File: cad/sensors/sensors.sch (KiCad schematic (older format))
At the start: 65 parts

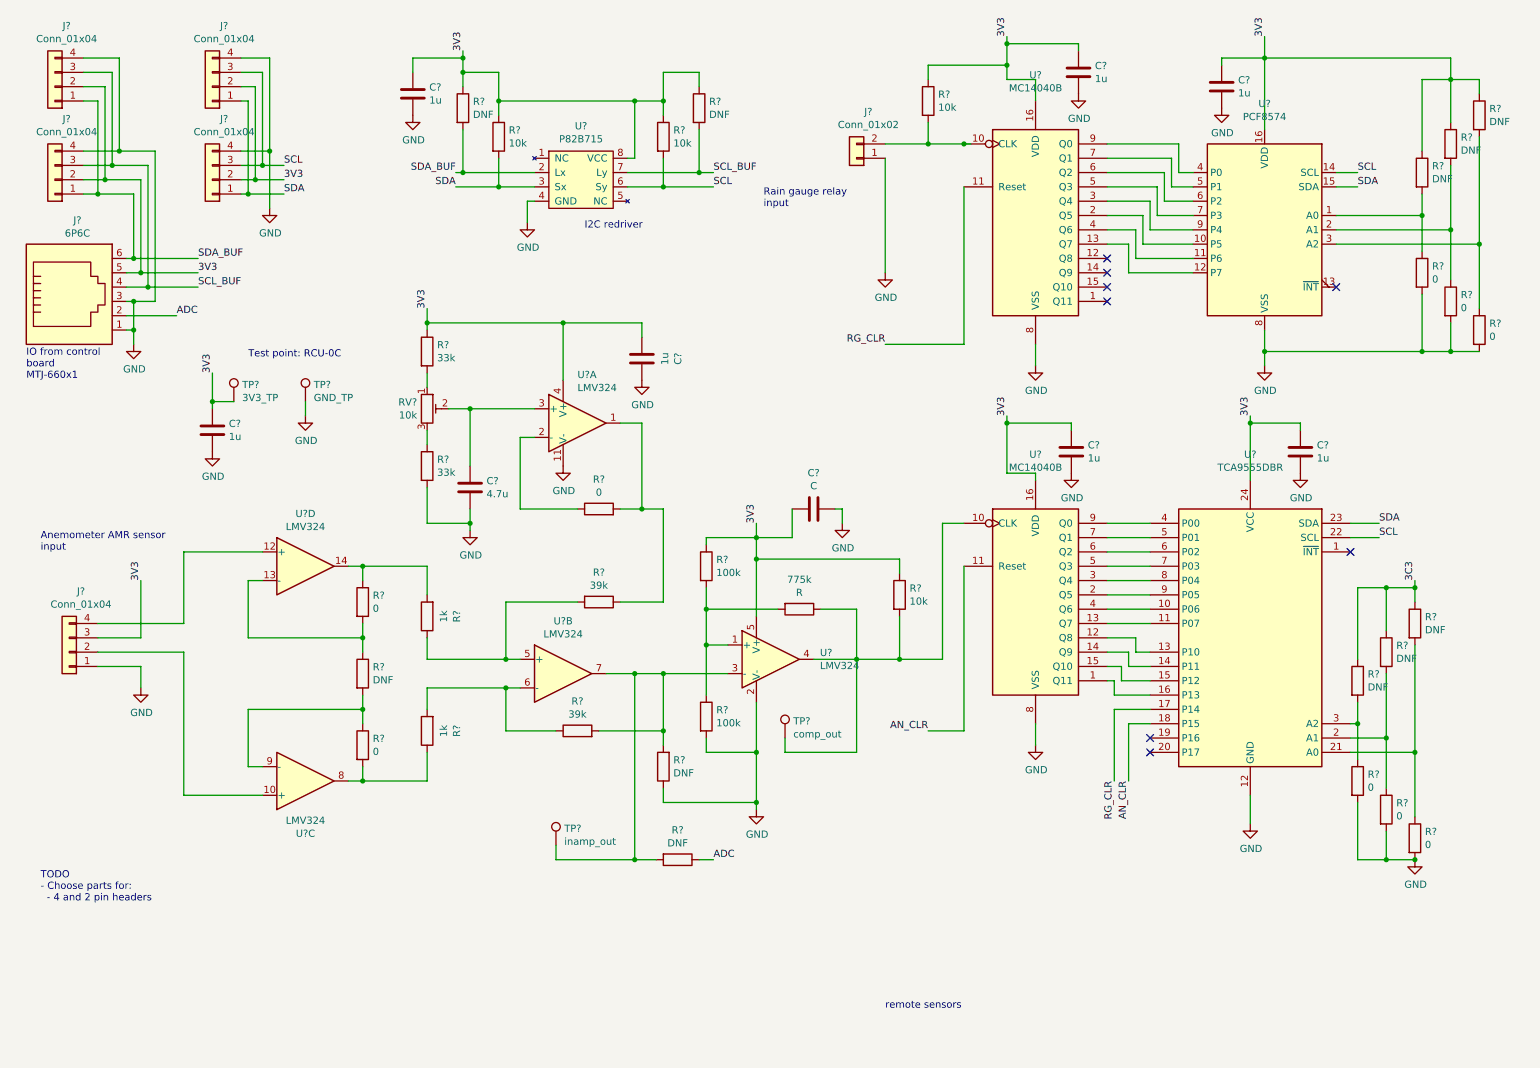
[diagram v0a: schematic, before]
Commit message: Added decoupling inductors and capacitors
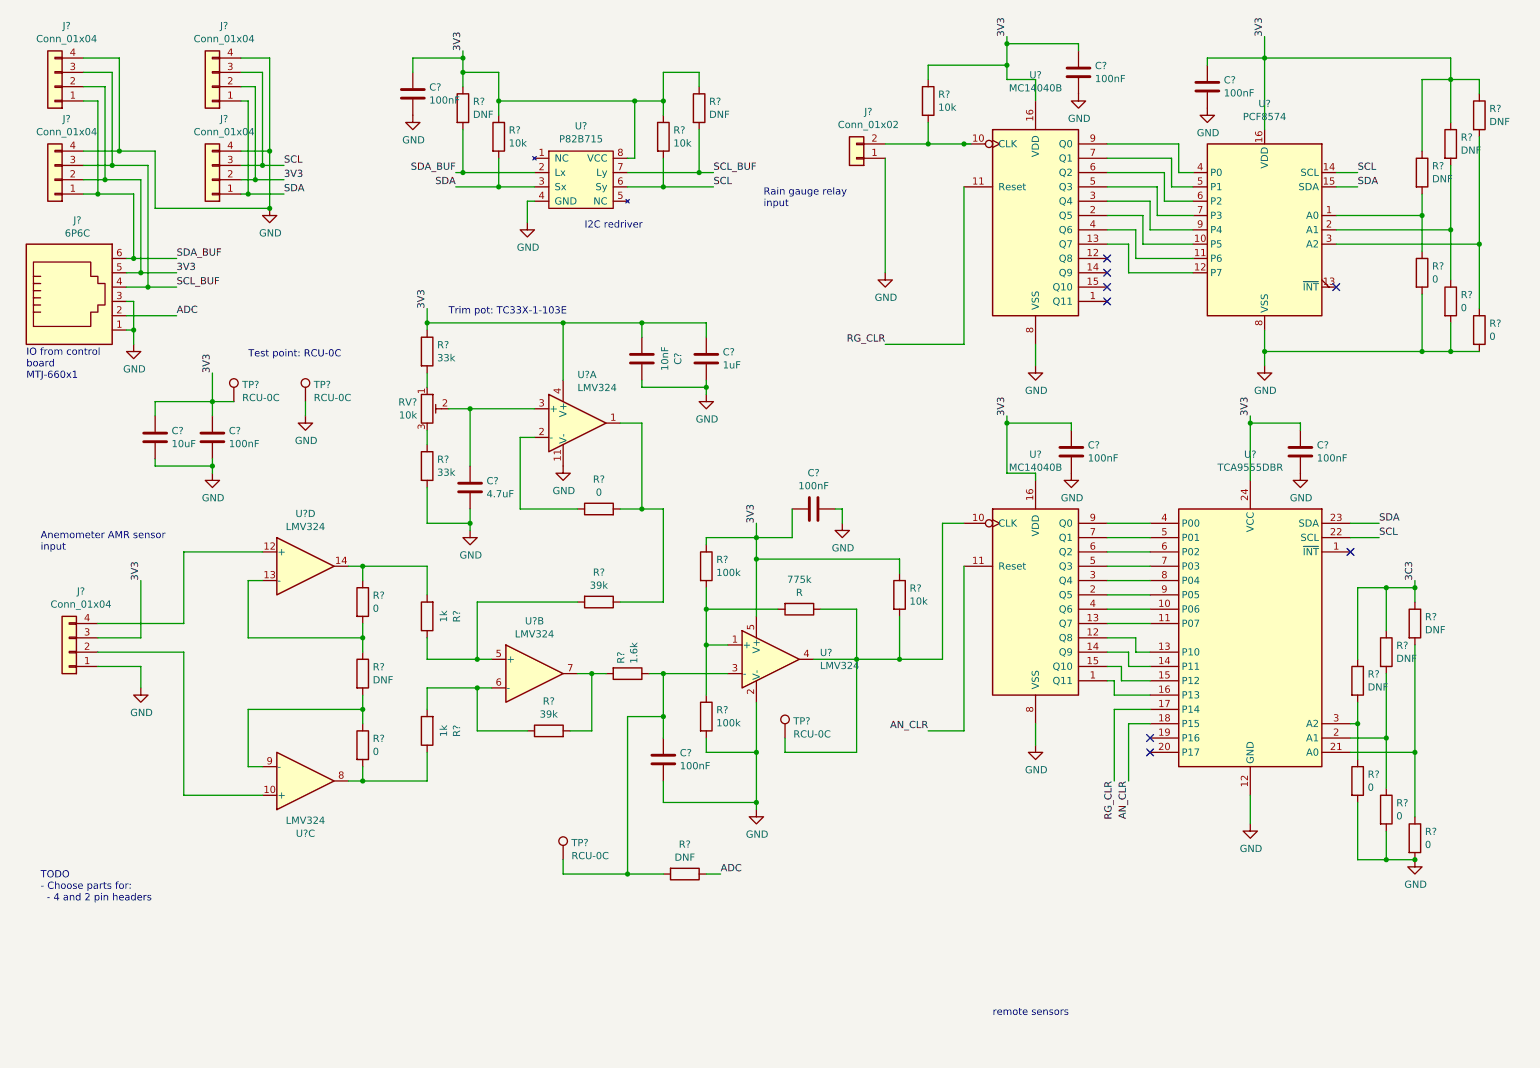
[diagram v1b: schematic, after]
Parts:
- removed R?: DNF, symbol Device:R
- added C?: 10uF, Capacitor_SMD:C_0603_1608Metric, symbol Device:C
- added C? (x2): 100nF, Capacitor_SMD:C_0603_1608Metric, symbol Device:C
- added R?: 1.6k, Resistor_SMD:R_0603_1608Metric, symbol Device:R
- 775k, R? (x31): footprint (none) -> Resistor_SMD:R_0603_1608Metric
- C?: value 1u -> 10nF; footprint (none) -> Capacitor_SMD:C_0603_1608Metric
- C?: value 4.7u -> 4.7uF; footprint (none) -> Capacitor_SMD:C_0603_1608Metric
- C?: value C -> 100nF; footprint (none) -> Capacitor_SMD:C_0603_1608Metric
- C? (x5): value 1u -> 100nF; footprint (none) -> Capacitor_SMD:C_0603_1608Metric
- C?: value 1u -> 1uF; footprint (none) -> Capacitor_SMD:C_0603_1608Metric
- TP?: value inamp_out -> RCU-0C
- TP?: value comp_out -> RCU-0C
- TP?: value 3V3_TP -> RCU-0C
- TP?: value GND_TP -> RCU-0C
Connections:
- net 3V3: now also C?.1, C?.1
- net GND: now also C?.1, C?.2, C?.2
- net at R?.2, TP?.1, U?.3 (-): now also C?.2, R?.1; no longer R?.2, U?.7
- new net: R?.2, R?.2, U?.7
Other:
- note added: "Trim pot: TC33X-1-103E"
- moved on the sheet: C?, R?, TP?, U?B

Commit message: Ordered components
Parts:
- R19: renamed from 775k; value R -> 775k
- U3: renamed from U?; value LMV324 -> LMV331
- gave numbers to parts that had none: 62

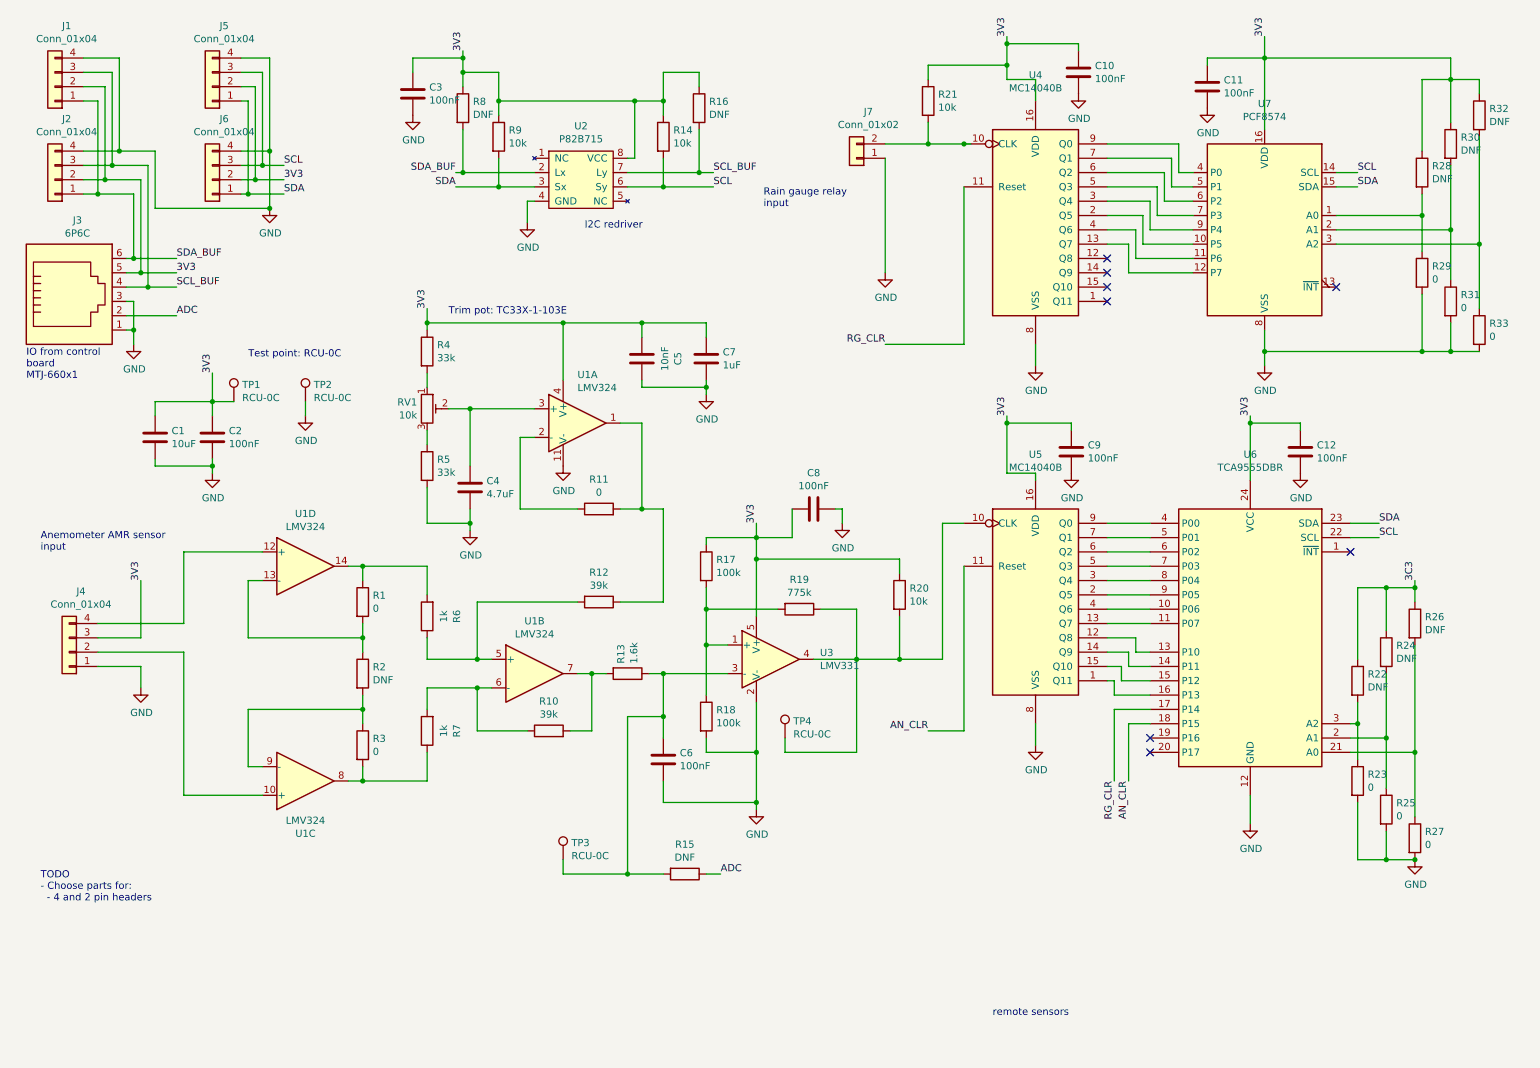
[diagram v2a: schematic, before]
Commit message: Changed I2C buffer to PCA1517, added termination network on RJ11 I2C lines
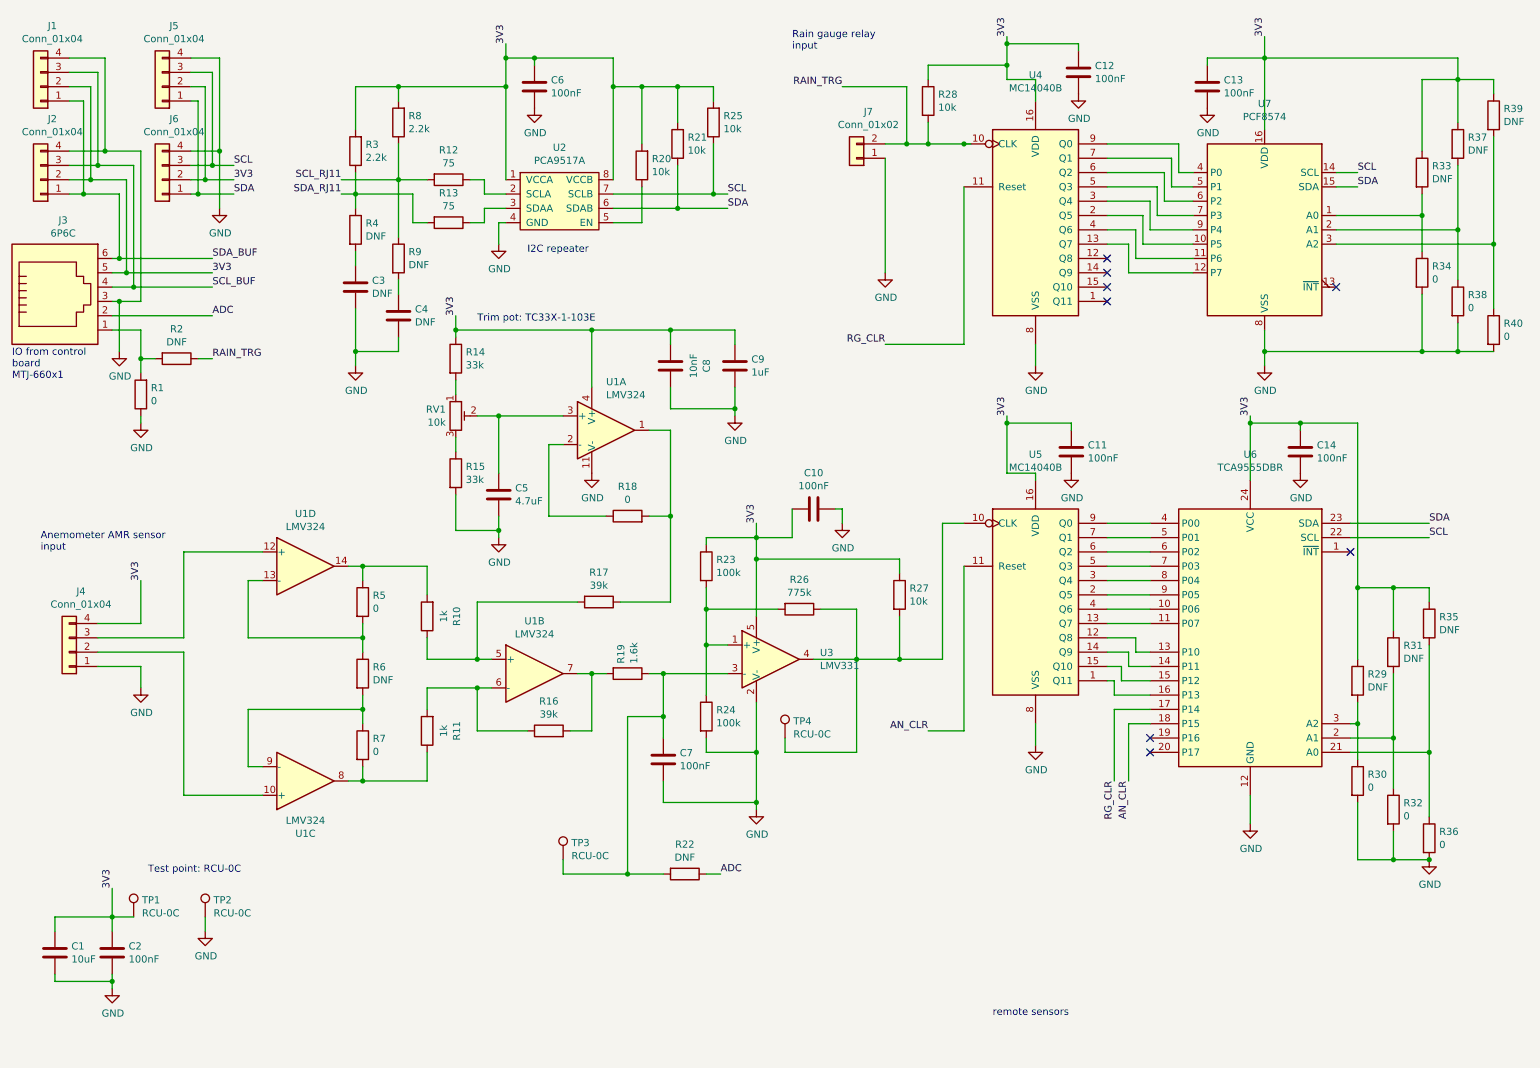
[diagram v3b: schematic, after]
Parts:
- removed R14: 10k, Resistor_SMD:R_0603_1608Metric, symbol Device:R
- removed R16: DNF, Resistor_SMD:R_0603_1608Metric, symbol Device:R
- removed U2: P82B715, symbol custom:P82B715
- added C4: DNF, Capacitor_SMD:C_0603_1608Metric, symbol Device:C
- added C6: 100nF, Capacitor_SMD:C_0603_1608Metric, symbol Device:C
- added R1: 0, Resistor_SMD:R_0603_1608Metric, symbol Device:R
- added R12, R13: 75, Resistor_SMD:R_0603_1608Metric, symbol Device:R
- added R2, R4: DNF, Resistor_SMD:R_0603_1608Metric, symbol Device:R
- added R20, R21, R25: 10k, Resistor_SMD:R_0603_1608Metric, symbol Device:R
- added R3: 2.2k, Resistor_SMD:R_0603_1608Metric, symbol Device:R
- added U2: PCA9517A, symbol custom:PCA9517A
- C3: value 100nF -> DNF
- R8: value DNF -> 2.2k
- R9: value 10k -> DNF
- renumbered C8 to C10, C9 to C11, C10 to C12, C11 to C13, C12 to C14, C4 to C5, C6 to C7, C5 to C8, C7 to C9, R6 to R10, R7 to R11, R4 to R14, R5 to R15, R10 to R16, R12 to R17, R11 to R18, R13 to R19, R15 to R22, R17 to R23, R18 to R24, R19 to R26, R20 to R27, R21 to R28, R22 to R29, R23 to R30, R24 to R31, R25 to R32, R28 to R33, R29 to R34, R26 to R35, R27 to R36, R30 to R37, R31 to R38, R32 to R39, R33 to R40, R1 to R5, R2 to R6, R3 to R7
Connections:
- net 3C3 is gone; now on net 3V3: R29.1, R31.1, R35.1
- net 3V3: now also J4.4 (Pin_4), R8.2, C6.1, R20.2, R21.2, R25.2, R3.2, U2.1 (VCCA), U2.8 (VCCB); no longer C3.2, J4.3 (Pin_3), R8.1, R9.1
- net GND: now also C3.2, C4.2, C6.2, R1.1, U2.4 (GND); no longer C3.1, J3.1
- net SCL: now also R25.1, U2.7 (SCLB)
- net SDA: now also R21.1, U2.6 (SDAB); no longer R9.2
- net SDA_BUF: no longer R8.2
- net RAIN_TRG: now reaches J7.2 (Pin_2), R28.2, U4.10 (CLK)
- net RAIN_TRG: now also R2.1
- net at U1.12 (+): now also J4.3 (Pin_3); no longer J4.4 (Pin_4)
- new net: J3.1, R1.2, R2.2
- new net: C4.1, R9.2
- new net: C3.1, R4.2
- new net: R12.1, U2.2 (SCLA)
- new net: R13.1, U2.3 (SDAA)
- new net: R20.1, U2.5 (EN)
- new net SCL_RJ11: R12.2, R8.1, R9.1
- new net SDA_RJ11: R13.2, R3.1, R4.1
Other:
- note added: "I2C repeater\n\n"
- note removed: "I2C redriver\n"
- note removed: "TODO\n- Choose parts for:\n - 4 and 2 pin headers"
- moved on the sheet: C1, C2, C5, C8, C9, J1, J2, J3, J5, J6, R14, R15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

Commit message: Final commit before moving to project repo
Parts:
- added C?: 100nF, Capacitor_SMD:C_0603_1608Metric, symbol Device:C
- added R?: 100k, Resistor_SMD:R_0603_1608Metric, symbol Device:R
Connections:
- net GND: now also C?.1
- net RAIN_TRG: now also C?.2, R?.1; no longer J7.2 (Pin_2), R28.2
- new net: J7.2 (Pin_2), R28.2, R?.2
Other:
- moved on the sheet: J7, R28
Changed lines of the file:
@@
 Wire Wire Line
 	7700 5450 7700 5600
-Wire Wire Line
-	7200 4350 7200 5500
 Text Label 7500 3300 1    50   ~ 0
 3V3
@@
 L Connector_Generic:Conn_01x02 J7
 U 1 1 6232698D
-P 6450 1500
-F 0 "J7" H 6368 1175 50  0000 C CNN
-F 1 "Conn_01x02" H 6368 1266 50  0000 C CNN
-F 2 "" H 6450 1500 50  0001 C CNN
-F 3 "~" H 6450 1500 50  0001 C CNN
-	1    6450 1500
+P 6000 1500
+F 0 "J7" H 5918 1175 50  0000 C CNN
+F 1 "Conn_01x02" H 5918 1266 50  0000 C CNN
+F 2 "" H 6000 1500 50  0001 C CNN
+F 3 "~" H 6000 1500 50  0001 C CNN
+	1    6000 1500
 	-1   0    0    1
 $EndComp
@@
 L power:GND #PWR015
 U 1 1 62326995
-P 6650 2300
-F 0 "#PWR015" H 6650 2050 50  0001 C CNN
-F 1 "GND" H 6655 2127 50  0000 C CNN
-F 2 "" H 6650 2300 50  0001 C CNN
-F 3 "" H 6650 2300 50  0001 C CNN
-	1    6650 2300
+P 6200 2300
+F 0 "#PWR015" H 6200 2050 50  0001 C CNN
+F 1 "GND" H 6205 2127 50  0000 C CNN
+F 2 "" H 6200 2300 50  0001 C CNN
+F 3 "" H 6200 2300 50  0001 C CNN
+	1    6200 2300
 	1    0    0    -1
 $EndComp
@@
 L Device:R R28
 U 1 1 6232699B
-P 6950 1100
-F 0 "R28" H 7020 1146 50  0000 L CNN
-F 1 "10k" H 7020 1055 50  0000 L CNN
-F 2 "Resistor_SMD:R_0603_1608Metric" V 6880 1100 50  0001 C CNN
-F 3 "~" H 6950 1100 50  0001 C CNN
-	1    6950 1100
+P 6350 1100
+F 0 "R28" H 6420 1146 50  0000 L CNN
+F 1 "10k" H 6420 1055 50  0000 L CNN
+F 2 "Resistor_SMD:R_0603_1608Metric" V 6280 1100 50  0001 C CNN
+F 3 "~" H 6350 1100 50  0001 C CNN
+	1    6350 1100
 	1    0    0    -1
 $EndComp
@@
 Wire Wire Line
 	8250 5350 8500 5350
-Connection ~ 7200 1400
 Wire Wire Line
 	7200 1400 7250 1400
@@
 NoConn ~ 8200 2500
 Wire Wire Line
-	7200 1700 7200 2800
-Wire Wire Line
-	7200 2800 6650 2800
-Text Label 6650 2800 2    50   ~ 0
+	7200 1700 7200 2650
+Text Label 6950 2650 2    50   ~ 0
 RG_CLR
-Text Label 6950 5500 2    50   ~ 0
+Text Label 7050 5200 2    50   ~ 0
 AN_CLR
 Wire Wire Line
@@
 	6000 4150 5750 4150
 Wire Wire Line
-	7200 5500 6950 5500
-Wire Wire Line
 	7200 4050 7050 4050
 Wire Wire Line
@@
 Rain gauge relay\ninput\n
 Wire Wire Line
-	6650 1500 6650 2300
-Wire Wire Line
-	6650 1400 6800 1400
-Wire Wire Line
-	6950 1250 6950 1400
-Connection ~ 6950 1400
-Wire Wire Line
-	6950 1400 7200 1400
-Wire Wire Line
-	6950 950  6950 850
-Wire Wire Line
-	6950 850  7500 850
+	6350 1250 6350 1400
+Wire Wire Line
+	6350 950  6350 850
 Wire Wire Line
 	1250 2200 1300 2200
@@
 Text Notes 7400 7500 0    50   ~ 0
 remote sensors
-Wire Wire Line
-	6800 1400 6800 1000
-Wire Wire Line
-	6800 1000 6350 1000
-Connection ~ 6800 1400
-Wire Wire Line
-	6800 1400 6950 1400
-Text Label 6350 1000 2    50   ~ 0
+Text Label 6950 2550 2    50   ~ 0
 RAIN_TRG
 $Comp
@@
 Wire Wire Line
 	5150 3100 5150 3250
+$Comp
+L Device:R R?
+U 1 1 625AA245
+P 6600 1400
+F 0 "R?" H 6670 1446 50  0000 L CNN
+F 1 "100k" H 6670 1355 50  0000 L CNN
+F 2 "Resistor_SMD:R_0603_1608Metric" V 6530 1400 50  0001 C CNN
+F 3 "~" H 6600 1400 50  0001 C CNN
+	1    6600 1400
+	0    1    1    0
+$EndComp
+Connection ~ 7200 1400
+Wire Wire Line
+	6200 1400 6350 1400
+$Comp
+L Device:C C?
+U 1 1 6268216E
+P 6800 1800
+F 0 "C?" H 6685 1754 50  0000 R CNN
+F 1 "100nF" H 6685 1845 50  0000 R CNN
+F 2 "Capacitor_SMD:C_0603_1608Metric" H 6838 1650 50  0001 C CNN
+F 3 "~" H 6800 1800 50  0001 C CNN
+	1    6800 1800
+	-1   0    0    1
+$EndComp
+Wire Wire Line
+	6350 850  7500 850
+Wire Wire Line
+	6350 1400 6450 1400
+Connection ~ 6350 1400
+Wire Wire Line
+	6750 1400 6800 1400
+Wire Wire Line
+	6800 1400 6800 1650
+Connection ~ 6800 1400
+Wire Wire Line
+	6800 1950 6800 2150
+Wire Wire Line
+	6200 1500 6200 2150
+Wire Wire Line
+	6800 2150 6200 2150
+Connection ~ 6200 2150
+Wire Wire Line
+	6200 2150 6200 2300
+Wire Wire Line
+	6950 2650 7200 2650
+Wire Wire Line
+	7200 4350 7200 5200
+Wire Wire Line
+	7200 5200 7050 5200
+Wire Wire Line
+	7150 2550 7150 1400
+Connection ~ 7150 1400
+Wire Wire Line
+	7150 1400 7200 1400
+Wire Wire Line
+	6800 1400 7150 1400
+Wire Wire Line
+	6950 2550 7150 2550
 $EndSCHEMATC

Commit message: Added custom libraries submodule and updated the symbol tables in the kicad projects
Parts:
- U2: symbol custom:PCA9517A -> custom_digital:PCA9517A
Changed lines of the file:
@@
 	1750 4250 1750 4850
 $Comp
-L custom:PCA9517A U2
+L custom_digital:PCA9517A U2
 U 1 1 62DAA650
 P 4400 1500
